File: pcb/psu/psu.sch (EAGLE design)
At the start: 32 parts, among them J1 BATTERY_CONNDEANS, U1 EEPROM-I2CSMD, U2 LM2596, U3 LM2596

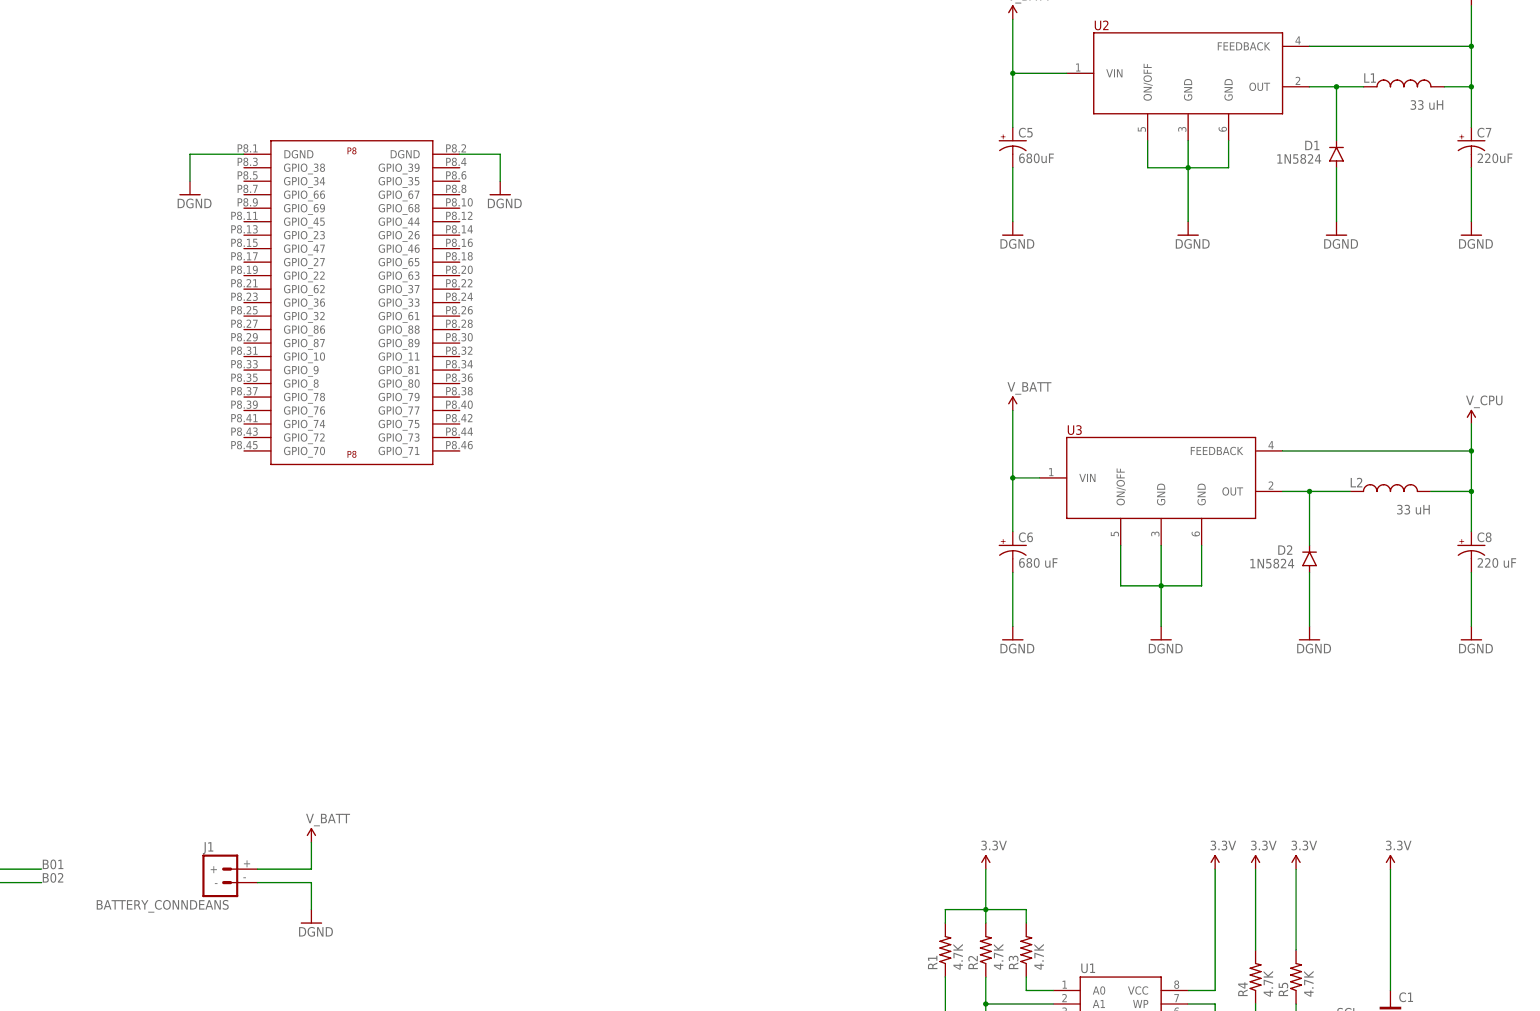
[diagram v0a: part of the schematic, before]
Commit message: Updated board layout and changed deans connector to screw terminal
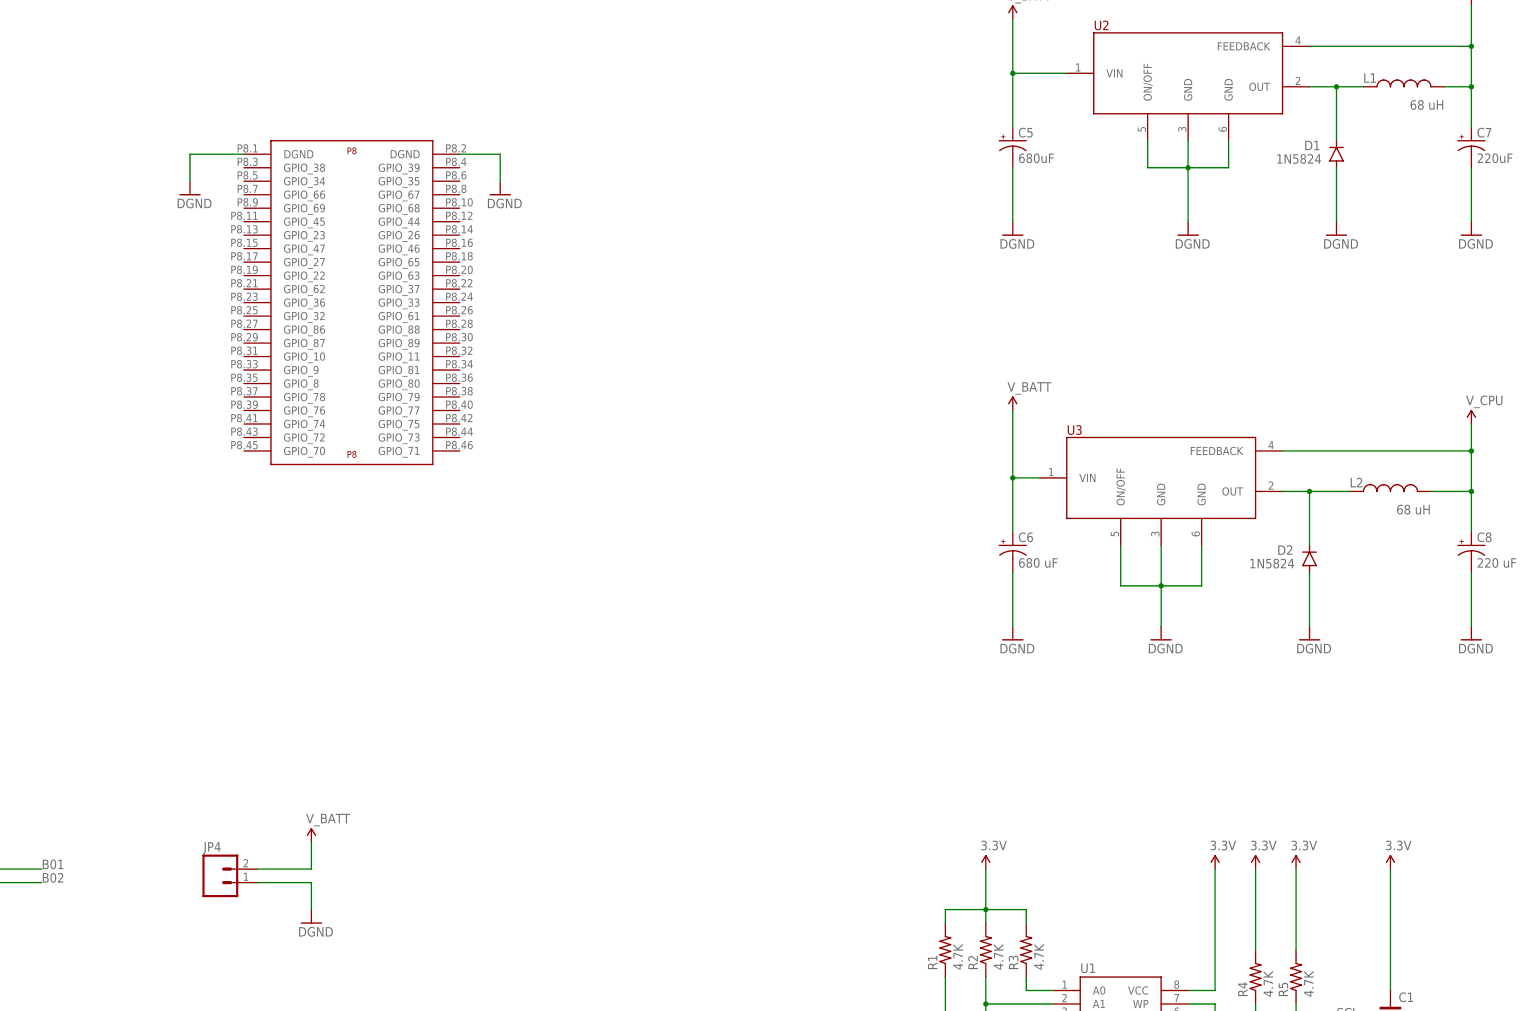
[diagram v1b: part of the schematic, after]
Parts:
- removed J1: BATTERY_CONNDEANS, SparkFun-Connectors:BATTERY_CONNDEANS
- added JP4: (no value), SparkFun-Connectors:M023.5MM
- L1, L2: value 33 uH -> 68 uH
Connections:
- net GND: now also JP4.1; no longer J1.-
- net V_BATT: now also JP4.2; no longer J1.+
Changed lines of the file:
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@@
 <part name="C7" library="SparkFun-Capacitors" deviceset="CAP_POL" device="PTH2" value="220uF"/>
 <part name="GND13" library="SparkFun-Aesthetics" deviceset="DGND" device=""/>
-<part name="L1" library="SparkFun-Passives" deviceset="INDUCTOR" device="0603" value="33 uH"/>
+<part name="L1" library="SparkFun-Passives" deviceset="INDUCTOR" device="0603" value="68 uH"/>
 <part name="D1" library="SparkFun-DiscreteSemi" deviceset="DIODE" device="PTH" value="1N5824"/>
 <part name="GND24" library="SparkFun-Aesthetics" deviceset="DGND" device=""/>
@@
 <part name="GND26" library="SparkFun-Aesthetics" deviceset="DGND" device=""/>
 <part name="C8" library="SparkFun-Capacitors" deviceset="CAP_POL" device="PTH2" value="220 uF"/>
-<part name="L2" library="SparkFun-Passives" deviceset="INDUCTOR" device="0603" value="33 uH"/>
+<part name="L2" library="SparkFun-Passives" deviceset="INDUCTOR" device="0603" value="68 uH"/>
 <part name="D2" library="SparkFun-DiscreteSemi" deviceset="DIODE" device="PTH" value="1N5824"/>
-<part name="J1" library="SparkFun-Connectors" deviceset="BATTERY_CONN" device="DEANS"/>
 <part name="SUPPLY21" library="SparkFun-Aesthetics" deviceset="V_BATT" device=""/>
 <part name="GND12" library="SparkFun-Aesthetics" deviceset="DGND" device=""/>
+<part name="JP4" library="SparkFun-Connectors" deviceset="M02" device="3.5MM"/>
 </parts>
 <sheets>
@@
 <attribute name="VALUE" x="380.7714" y="165.1" size="1.778" layer="96" rot="R180"/>
 </instance>
-<instance part="J1" gate="G$1" x="177.8" y="106.68" smashed="yes">
-<attribute name="VALUE" x="154.94" y="99.06" size="1.778" layer="96"/>
-<attribute name="NAME" x="175.26" y="109.982" size="1.778" layer="95"/>
-</instance>
 <instance part="SUPPLY21" gate="G$1" x="195.58" y="111.76"/>
 <instance part="GND12" gate="G$1" x="195.58" y="96.52"/>
+<instance part="JP4" gate="G$1" x="177.8" y="104.14"/>
 </instances>
 <busses>
@@
 <wire x1="195.58" y1="99.06" x2="195.58" y2="104.14" width="0.1524" layer="91"/>
 <wire x1="195.58" y1="104.14" x2="185.42" y2="104.14" width="0.1524" layer="91"/>
-<pinref part="J1" gate="G$1" pin="-"/>
+<pinref part="JP4" gate="G$1" pin="1"/>
 </segment>
 </net>
@@
 </segment>
 <segment>
-<pinref part="J1" gate="G$1" pin="+"/>
 <pinref part="SUPPLY21" gate="G$1" pin="V_BATT"/>
 <wire x1="185.42" y1="106.68" x2="195.58" y2="106.68" width="0.1524" layer="91"/>
 <wire x1="195.58" y1="106.68" x2="195.58" y2="111.76" width="0.1524" layer="91"/>
-</segment>
-</net>
+<pinref part="JP4" gate="G$1" pin="2"/>
+</segment>
+</net>

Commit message: Lots of routing tweaks
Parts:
- added R10, R7: 0, SparkFun-Resistors:RESISTOR0603
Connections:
- new net SCL_PRE: R4.1, R7.1, U1.SCL
- new net SDA_PRE: R10.1, R5.1, U1.SDA
- net SCL: now also R7.2; no longer R4.1, U1.SCL
- net SDA: now also R10.2; no longer R5.1, U1.SDA
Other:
- moved on the sheet: C1
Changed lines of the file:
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@@
 <part name="GND12" library="SparkFun-Aesthetics" deviceset="DGND" device=""/>
 <part name="JP4" library="SparkFun-Connectors" deviceset="M02" device="3.5MM"/>
+<part name="R7" library="SparkFun-Resistors" deviceset="RESISTOR" device="0603" value="0"/>
+<part name="R10" library="SparkFun-Resistors" deviceset="RESISTOR" device="0603" value="0"/>
 </parts>
 <sheets>
@@
 <instances>
 <instance part="U1" gate="G$1" x="347.98" y="78.74"/>
-<instance part="SUPPLY1" gate="G$1" x="398.78" y="106.68"/>
-<instance part="GND1" gate="G$1" x="398.78" y="55.88"/>
+<instance part="SUPPLY1" gate="G$1" x="297.18" y="106.68"/>
+<instance part="GND1" gate="G$1" x="297.18" y="55.88"/>
 <instance part="R1" gate="G$1" x="314.96" y="91.44" rot="R90"/>
 <instance part="R2" gate="G$1" x="322.58" y="91.44" rot="R90"/>
@@
 <instance part="R5" gate="G$1" x="381" y="86.36" rot="R90"/>
 <instance part="R6" gate="G$1" x="365.76" y="68.58" rot="R90"/>
-<instance part="C1" gate="G$1" x="398.78" y="78.74"/>
+<instance part="C1" gate="G$1" x="297.18" y="78.74"/>
 <instance part="GND4" gate="G$1" x="172.72" y="233.68"/>
 <instance part="GND6" gate="G$1" x="332.74" y="66.04"/>
@@
 <instance part="GND12" gate="G$1" x="195.58" y="96.52"/>
 <instance part="JP4" gate="G$1" x="177.8" y="104.14"/>
+<instance part="R7" gate="G$1" x="393.7" y="78.74" smashed="yes">
+<attribute name="NAME" x="389.89" y="80.2386" size="1.778" layer="95"/>
+</instance>
+<instance part="R10" gate="G$1" x="393.7" y="76.2" smashed="yes">
+<attribute name="NAME" x="389.89" y="72.6186" size="1.778" layer="95"/>
+</instance>
 </instances>
 <busses>
@@
 <pinref part="C1" gate="G$1" pin="1"/>
 <pinref part="SUPPLY1" gate="G$1" pin="3.3V"/>
-<wire x1="398.78" y1="83.82" x2="398.78" y2="106.68" width="0.1524" layer="91"/>
+<wire x1="297.18" y1="83.82" x2="297.18" y2="106.68" width="0.1524" layer="91"/>
 </segment>
 <segment>
@@
 <pinref part="GND1" gate="G$1" pin="GND"/>
 <pinref part="C1" gate="G$1" pin="2"/>
-<wire x1="398.78" y1="58.42" x2="398.78" y2="76.2" width="0.1524" layer="91"/>
+<wire x1="297.18" y1="58.42" x2="297.18" y2="76.2" width="0.1524" layer="91"/>
 </segment>
 <segment>
@@
 <net name="SCL" class="0">
 <segment>
-<pinref part="U1" gate="G$1" pin="SCL"/>
-<wire x1="360.68" y1="78.74" x2="373.38" y2="78.74" width="0.1524" layer="91"/>
-<pinref part="R4" gate="G$1" pin="1"/>
-<wire x1="373.38" y1="78.74" x2="373.38" y2="81.28" width="0.1524" layer="91"/>
-<wire x1="373.38" y1="78.74" x2="388.62" y2="78.74" width="0.1524" layer="91"/>
-<junction x="373.38" y="78.74"/>
-<label x="388.62" y="78.74" size="1.778" layer="95"/>
-</segment>
-<segment>
 <pinref part="U$1" gate="P9" pin="I2C2_SCL"/>
 <wire x1="55.88" y1="218.44" x2="43.18" y2="218.44" width="0.1524" layer="91"/>
 <label x="38.1" y="218.44" size="1.778" layer="95"/>
 </segment>
+<segment>
+<pinref part="R7" gate="G$1" pin="2"/>
+<wire x1="398.78" y1="78.74" x2="406.4" y2="78.74" width="0.1524" layer="91"/>
+<label x="406.4" y="78.74" size="1.778" layer="95"/>
+</segment>
 </net>
 <net name="SDA" class="0">
-<segment>
-<pinref part="U1" gate="G$1" pin="SDA"/>
-<wire x1="360.68" y1="76.2" x2="381" y2="76.2" width="0.1524" layer="91"/>
-<pinref part="R5" gate="G$1" pin="1"/>
-<wire x1="381" y1="76.2" x2="381" y2="81.28" width="0.1524" layer="91"/>
-<label x="388.62" y="76.2" size="1.778" layer="95"/>
-<wire x1="381" y1="76.2" x2="388.62" y2="76.2" width="0.1524" layer="91"/>
-<junction x="381" y="76.2"/>
-</segment>
 <segment>
 <pinref part="U$1" gate="P9" pin="I2C2_SDA"/>
 <wire x1="96.52" y1="218.44" x2="106.68" y2="218.44" width="0.1524" layer="91"/>
 <label x="106.68" y="218.44" size="1.778" layer="95"/>
+</segment>
+<segment>
+<pinref part="R10" gate="G$1" pin="2"/>
+<wire x1="398.78" y1="76.2" x2="406.4" y2="76.2" width="0.1524" layer="91"/>
+<label x="406.4" y="76.2" size="1.778" layer="95"/>
 </segment>
 </net>
@@
 </segment>
 </net>
+<net name="SCL_PRE" class="0">
+<segment>
+<pinref part="U1" gate="G$1" pin="SCL"/>
+<wire x1="360.68" y1="78.74" x2="373.38" y2="78.74" width="0.1524" layer="91"/>
+<pinref part="R4" gate="G$1" pin="1"/>
+<wire x1="373.38" y1="78.74" x2="373.38" y2="81.28" width="0.1524" layer="91"/>
+<wire x1="373.38" y1="78.74" x2="388.62" y2="78.74" width="0.1524" layer="91"/>
+<junction x="373.38" y="78.74"/>
+<pinref part="R7" gate="G$1" pin="1"/>
+</segment>
+</net>
+<net name="SDA_PRE" class="0">
+<segment>
+<pinref part="U1" gate="G$1" pin="SDA"/>
+<wire x1="360.68" y1="76.2" x2="381" y2="76.2" width="0.1524" layer="91"/>
+<pinref part="R5" gate="G$1" pin="1"/>
+<wire x1="381" y1="76.2" x2="381" y2="81.28" width="0.1524" layer="91"/>
+<wire x1="381" y1="76.2" x2="388.62" y2="76.2" width="0.1524" layer="91"/>
+<junction x="381" y="76.2"/>
+<pinref part="R10" gate="G$1" pin="1"/>
+</segment>
+</net>
